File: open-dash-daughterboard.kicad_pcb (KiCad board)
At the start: 2 copper layers, 165.5 x 107.3 mm, 161 parts, among them J4 Conn_02x06_Odd_Even, P1 CONN_01X04, P2 CONN_01X02, P4 CONN_01X04, Q1 Q_NPN_BEC, Q2 Q_NJFET_DGS, Q3 Q_NJFET_DGS, Q4 Q_NPN_BCE, Q5 Q_PNP_BCE, U1 LM2576-ADJ, U10 Power-Monitor-INA219, U11 TDA7297, U12 Si4740, U13 A2235-H, U14 molex-2x4-5.7mm, U15 radio-housing-mounts, U16 molex-2x4-5.7mm, U17 USB_IC-CP2104, U18 74LVC1G17SE-7, U19 OPA1662, U2 LM2576-ADJ, U3 LM2576-ADJ, U4 LM2576-ADJ, U5 REG-3.3v, U6 ESP-WROOM-32, U7 molex-2x4-5.7mm, U8 MCP2551-I_SN, U9 SI7020-A20

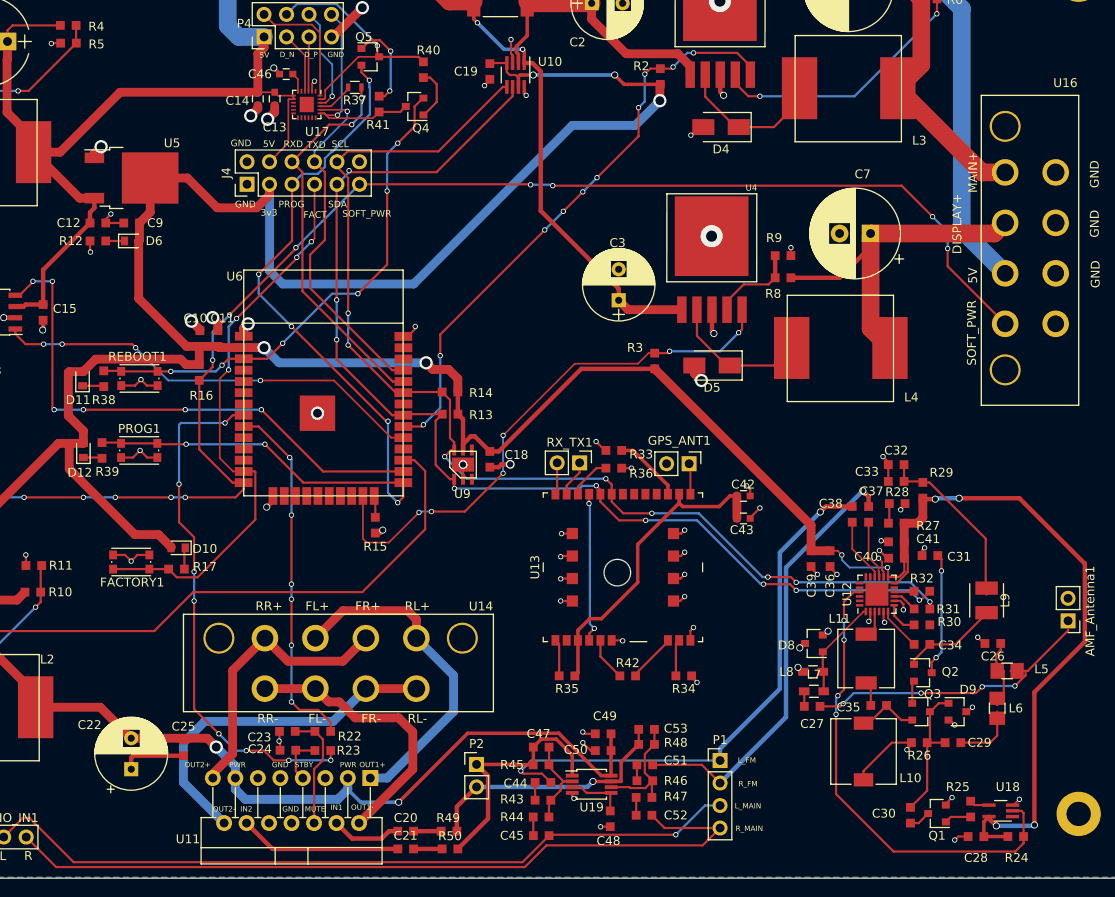
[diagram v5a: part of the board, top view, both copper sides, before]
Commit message: added softpower circuit
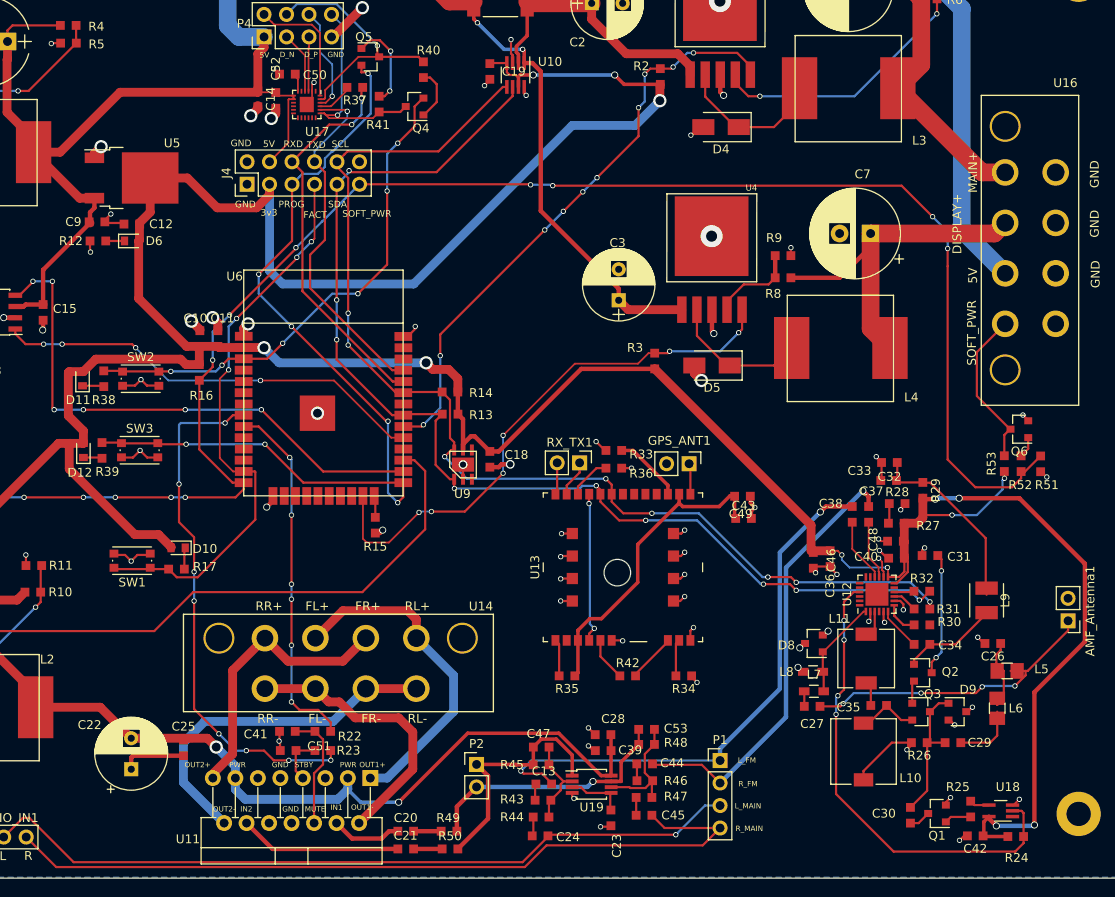
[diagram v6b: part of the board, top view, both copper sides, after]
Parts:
- removed FACTORY1, PROG1, REBOOT1: SW_PUSH, Buttons_Switches_SMD:SW_SPST_KMR2
- added Q6: Q_NPN_BEC, Package_TO_SOT_SMD:SOT-23, F.Cu at (215.3, 96.6)
- added R51: R_1k, Resistor_SMD:R_0603_1608Metric_Pad0.99x1.00mm_HandSolder, F.Cu at (217.7, 100.5)
- added R52: R_1k, Resistor_SMD:R_0603_1608Metric_Pad0.99x1.00mm_HandSolder, F.Cu at (215.5, 100.5)
- added R53: R_1k, Resistor_SMD:R_0603_1608Metric_Pad0.99x1.00mm_HandSolder, F.Cu at (213.6, 100.5)
- added SW1: SW_PUSH, Button_Switch_SMD:SW_SPST_KMR2, F.Cu at (115.1, 111.5)
- added SW2: SW_PUSH, Button_Switch_SMD:SW_SPST_KMR2, F.Cu at (116.1, 90.9)
- added SW3: SW_PUSH, Button_Switch_SMD:SW_SPST_KMR2, F.Cu at (116.0, 99.0)
- C11: value C_1uF -> C_4.7uF
- C12: value C_4.7uF -> C_1uF
- C13, C14, C43: footprint Capacitors_SMD:C_0603 -> Capacitor_SMD:C_0603_1608Metric_Pad0.99x1.00mm_HandSolder
- C15, C39: value 0.1uF -> C_0.1uF
- C25: value 100nF -> C_0.1uF
- C28, C41: value 0.1uF -> C_1uF
- C32: value 100uF -> C_47uF
- C42, C46: value C_1uF -> C_0.1uF; footprint Capacitors_SMD:C_0603 -> Capacitor_SMD:C_0603_1608Metric_Pad0.99x1.00mm_HandSolder
- C48: value C_1uF -> C_0.1uF
- C50: value C_0.1uF -> C_1uF
- R11: value R_1k3 -> R_1.3K
- R18, R24: value 4.7k -> R_4K7
- R29: value 10 -> R_10
- R37: footprint Resistors_SMD:R_0603 -> Resistor_SMD:R_0603_1608Metric_Pad0.99x1.00mm_HandSolder
- U1, U2, U3, U4: value LM2576-ADJ -> LM2576
- moved C52 90.8 mm to (131.3, 59.5), turned to 270 degrees
- moved C50 84.3 mm to (132.6, 56.5), turned to 0 degrees
- moved C13 83.1 mm to (161.6, 136.7), turned to 0 degrees
- moved C46 81.0 mm to (192.0, 111.4), turned to 270 degrees
- moved C41 72.0 mm to (132.6, 130.7), turned to 180 degrees
- moved C42 46.5 mm to (210.3, 142.5), turned to 180 degrees
- moved C48 44.9 mm to (201.3, 109.3), turned to 180 degrees
- moved C28 43.7 mm to (168.3, 131.1), turned to 180 degrees
- moved C51 40.3 mm to (132.7, 132.9)
- moved C23 37.8 mm to (169.2, 140.5), turned to 270 degrees
- moved C39 32.0 mm to (168.3, 132.9), turned to 180 degrees
- moved C49 31.1 mm to (184.0, 104.2), turned to 0 degrees
- moved C24 30.1 mm to (161.2, 142.5), turned to 0 degrees
- moved C45 11.8 mm to (172.9, 140.2), turned to 180 degrees
- moved C44 11.7 mm to (173.0, 134.4), turned to 180 degrees
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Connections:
- C12 pad 1: /5V -> /3v3
- C13 pad 1: /5V -> Net-(C13-Pad1)
- C13 pad 2: AGND -> /L_FM_AUDIO
- C19 pad 1: AGND -> /3v3
- C19 pad 2: /3v3 -> AGND
- C24 pad 2: AGND -> /L_MAIN_AUDIO
- C28 pad 1: AGND -> /AUDIO_POWER
- C28 pad 2: /3v3 -> AGND
- C32 pad 1: Net-(C32-Pad1) -> AGND
- C32 pad 2: AGND -> Net-(C32-Pad2)
- C33 pad 1: Net-(C32-Pad1) -> Net-(C32-Pad2)
- C39 pad 1: AGND -> /AUDIO_POWER
- C39 pad 2: /3v3 -> AGND
- C41 pad 1: AGND -> Net-(C41-Pad1)
- C41 pad 2: /3v3 -> AGND
- C42 pad 1: /GPS interface/3v3 -> /3v3
- C44 pad 1: Net-(C44-Pad1) -> /R_FM_AUDIO
- C44 pad 2: /L_FM_AUDIO -> Net-(C44-Pad2)
- C45 pad 1: Net-(C45-Pad1) -> /R_MAIN_AUDIO
- C45 pad 2: /L_MAIN_AUDIO -> Net-(C45-Pad2)
- C46 pad 1: AGND -> /3v3
- C46 pad 2: Net-(C46-Pad2) -> AGND
- C48 pad 1: Net-(C48-Pad1) -> /3v3
- C49 pad 1: /AUDIO_POWER -> /GPS interface/3v3
- C50 pad 1: /AUDIO_POWER -> AGND
- C50 pad 2: AGND -> Net-(C50-Pad2)
- C51 pad 1: /R_FM_AUDIO -> Net-(C51-Pad1)
- C51 pad 2: Net-(C51-Pad2) -> AGND
- C52 pad 1: /R_MAIN_AUDIO -> /5V
- C52 pad 2: Net-(C52-Pad2) -> AGND
- C9 pad 1: /3v3 -> /5V
- L9 pad 1: Net-(C32-Pad1) -> Net-(C32-Pad2)
- R22 pad 1: Net-(C23-Pad1) -> Net-(C41-Pad1)
- R23 pad 1: Net-(C24-Pad1) -> Net-(C51-Pad1)
- R29 pad 1: Net-(C32-Pad1) -> Net-(C32-Pad2)
- R43 pad 2: Net-(C44-Pad1) -> Net-(C13-Pad1)
- R44 pad 2: Net-(C45-Pad1) -> Net-(C24-Pad1)
- R46 pad 1: Net-(C51-Pad2) -> Net-(C44-Pad2)
- R47 pad 1: Net-(C52-Pad2) -> Net-(C45-Pad2)
- U11 pad 6: Net-(C23-Pad1) -> Net-(C41-Pad1)
- U11 pad 7: Net-(C24-Pad1) -> Net-(C51-Pad1)
- U16 pad 4: /SOFT_POWER -> Net-(Q6-Pad3)
- U17 pad 25: Net-(U17-Pad25) -> AGND
- U17 pad 6: Net-(C46-Pad2) -> Net-(C50-Pad2)
- U19 pad 3: Net-(C48-Pad1) -> Net-(C23-Pad1)
- U19 pad 5: Net-(C48-Pad1) -> Net-(C23-Pad1)
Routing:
- net /SOFT_POWER: track 184.5 -> 210.8 mm
- net Net-(C32-Pad2): track 0.00 -> 21.1 mm
- net Net-(C32-Pad1): track 20.2 -> 0.00 mm
- net Net-(Q6-Pad3): track 0.00 -> 17.6 mm
- net Net-(C41-Pad1): track 0.00 -> 12.9 mm
- net /3v3: track 400.2 -> 412.6 mm, vias 11 -> 13
- net Net-(C48-Pad1): track 6.75 -> 0.00 mm
- net Net-(C23-Pad1): track 13.4 -> 6.75 mm
- net Net-(C51-Pad1): track 0.00 -> 6.60 mm
- net AGND: track 152.7 -> 157.4 mm, vias 87 -> 88
- net Net-(C24-Pad1): track 6.60 -> 2.11 mm
- net Net-(U17-Pad25): track 2.47 -> 0.00 mm
- net Net-(Q6-Pad1): track 0.00 -> 2.39 mm
- net Net-(C50-Pad2): track 0.00 -> 2.17 mm
- net Net-(C46-Pad2): track 2.17 -> 0.00 mm
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
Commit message: finished schematic, starting layout
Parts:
- removed AMF_Antenna1, GPS_ANT1: Conn_01x02, Connector_PinHeader_2.54mm:PinHeader_1x02_P2.54mm_Vertical
- removed AUDIO_IN1: Conn_01x02, Connector_PinHeader_2.54mm:PinHeader_1x03_P2.54mm_Vertical
- removed C10, C13, C24, C44, C45, C51, C52: C_10uF, Capacitor_SMD:C_0603_1608Metric_Pad0.99x1.00mm_HandSolder
- removed C11, C9: C_4.7uF, Capacitor_SMD:C_0603_1608Metric_Pad0.99x1.00mm_HandSolder
- removed C12, C23, C28, C41, C49, C50: C_1uF, Capacitor_SMD:C_0603_1608Metric_Pad0.99x1.00mm_HandSolder
- removed C14, C15, C18, C19, C25, C39, C42, C43, C46, C48: C_0.1uF, Capacitor_SMD:C_0603_1608Metric_Pad0.99x1.00mm_HandSolder
- removed C16, C17: 560pF, Capacitor_SMD:C_0603_1608Metric_Pad0.99x1.00mm_HandSolder
- removed C20, C21: 0.22uF, Capacitor_SMD:C_0603_1608Metric_Pad0.99x1.00mm_HandSolder
- removed C22: 470uF, Capacitor_THT:CP_Radial_D8.0mm_P3.50mm
- removed C26: 3.9pF, Capacitor_SMD:C_0603_1608Metric_Pad0.99x1.00mm_HandSolder
- removed C27: 18pF, Capacitor_SMD:C_0603_1608Metric_Pad0.99x1.00mm_HandSolder
- removed C30: 1200pF, Capacitor_SMD:C_0603_1608Metric_Pad0.99x1.00mm_HandSolder
- removed C31, C33, C34: 0.47uF, Capacitor_SMD:C_0603_1608Metric_Pad0.99x1.00mm_HandSolder
- removed C32: C_47uF, Capacitor_SMD:C_0603_1608Metric_Pad0.99x1.00mm_HandSolder
- removed C35: 18nF, Capacitor_SMD:C_0603_1608Metric_Pad0.99x1.00mm_HandSolder
- removed C36, C40: 22nF, Capacitor_SMD:C_0603_1608Metric_Pad0.99x1.00mm_HandSolder
- removed C37, C38: 0.39uF, Capacitor_SMD:C_0603_1608Metric_Pad0.99x1.00mm_HandSolder
- removed C47, C53: C_100p, Capacitor_SMD:C_0603_1608Metric_Pad0.99x1.00mm_HandSolder
- removed C7, C8: C_1000uF, Capacitor_THT:CP_Radial_D10.0mm_P3.50mm
- removed D1: 26V Zener, Diodes_SMD:D_SMB
- removed D10, D11, D12: LED, LED_SMD:LED_0603_1608Metric_Pad0.82x1.00mm_HandSolder
- removed D2, D3, D4, D5: D_Schottky, Diode_SMD:D_SMA
- removed D6: LED-0603-G, LED_SMD:LED_0603_1608Metric_Pad0.82x1.00mm_HandSolder
- removed D8, D9: D1213A-01SO-7, TO_SOT_Packages_SMD:SOT-23
- removed L1: L_47uH, open-automation:Inductor-SRR1210
- removed L10: 1mH, Inductors_SMD:L_7.3x7.3_H4.5
- removed L11: 33uH, Inductors_SMD:L_6.3x6.3_H3
- removed L2, L3, L4: L_100uH, open-automation:Inductor-SRR1210
- removed L5, L6: 6.8uH, open-automation:Coilcraft_0805PS_Handsoldering
- removed L7: 33nH, Inductors_SMD:L_0603_HandSoldering
- removed L8: 122nH, Inductors_SMD:L_0603_HandSoldering
- removed L9: 220uH, open-automation:Coilcraft_1008PS_Handsoldering
- removed P4: CONN_01X04, Connector_PinHeader_2.54mm:PinHeader_2x04_P2.54mm_Vertical
- removed Q3: Q_NJFET_DGS, TO_SOT_Packages_SMD:SOT-23
- removed Q4: Q_NPN_BCE, Package_TO_SOT_SMD:SOT-23
- removed Q5: Q_PNP_BCE, Package_TO_SOT_SMD:SOT-23
- removed Q6: Q_NPN_BEC, Package_TO_SOT_SMD:SOT-23
- removed R10: R_7k15, Resistor_SMD:R_0603_1608Metric_Pad0.99x1.00mm_HandSolder
- removed R11: R_1.3K, Resistor_SMD:R_0603_1608Metric_Pad0.99x1.00mm_HandSolder
- removed R12: R_1k4, Resistor_SMD:R_0603_1608Metric_Pad0.99x1.00mm_HandSolder
- removed R13, R14, R15, R16, R17, R22, R23, R33, R34, R35, R36, R38, R39, R42: R_10k, Resistor_SMD:R_0603_1608Metric_Pad0.99x1.00mm_HandSolder
- removed R18, R24: R_4K7, Resistor_SMD:R_0603_1608Metric_Pad0.99x1.00mm_HandSolder
- removed R19, R20: 100, Resistor_SMD:R_0603_1608Metric_Pad0.99x1.00mm_HandSolder
- removed R21: R_10, Resistor_SMD:R_2512_6332Metric_Pad1.49x3.40mm_HandSolder
- removed R25, R27, R28: 249, Resistor_SMD:R_0603_1608Metric_Pad0.99x1.00mm_HandSolder
- removed R26: 10M, Resistor_SMD:R_0603_1608Metric_Pad0.99x1.00mm_HandSolder
- removed R29: R_10, Resistor_SMD:R_0603_1608Metric_Pad0.99x1.00mm_HandSolder
- removed R30, R31, R32: 2k, Resistor_SMD:R_0603_1608Metric_Pad0.99x1.00mm_HandSolder
- removed R37: R_470, Resistor_SMD:R_0603_1608Metric_Pad0.99x1.00mm_HandSolder
- removed R40, R41: R_12k, Resistor_SMD:R_0603_1608Metric_Pad0.99x1.00mm_HandSolder
- removed R43, R44, R45, R46, R47, R48, R49, R50: R_20k, Resistor_SMD:R_0603_1608Metric_Pad0.99x1.00mm_HandSolder
- removed R5: R_2k32, Resistor_SMD:R_0603_1608Metric_Pad0.99x1.00mm_HandSolder
- removed R51, R52, R53, R7, R9: R_1k, Resistor_SMD:R_0603_1608Metric_Pad0.99x1.00mm_HandSolder
- removed R8: R_8k87, Resistor_SMD:R_0603_1608Metric_Pad0.99x1.00mm_HandSolder
- removed RX_TX1: CONN_01X02, Connector_PinHeader_2.54mm:PinHeader_1x02_P2.54mm_Vertical
- removed SW1, SW2, SW3: SW_PUSH, Button_Switch_SMD:SW_SPST_KMR2
- removed U10: Power-Monitor-INA219, TO_SOT_Packages_SMD:SOT-23-8_Handsoldering
- removed U11: TDA7297, Package_TO_SOT_THT:TO-220-15_Vertical_StaggeredType1_Py5.08mm
- removed U14, U16: molex-2x4-5.7mm, open-automation:molex-2x4-5.7mm
- removed U15: radio-housing-mounts, open-automation:radio-housing-mounts
- removed U17: USB_IC-CP2104, Housings_DFN_QFN:QFN-24-1EP_3x3mm_Pitch0.4mm
- removed U18: 74LVC1G17SE-7, TO_SOT_Packages_SMD:SOT-353_SC-70-5_Handsoldering
- removed U19: OPA1662, Package_SO:MSOP-8_3x3mm_P0.65mm
- removed U9: SI7020-A20, open-automation:SI7020-A20
- added J1: RCA-PJRAN1X1U04X, open-automation:RCA-PJRAN1X1U04X, F.Cu at (114.8, 294.8)
- added J2: AudioJack4_TTRS, open-automation:AudioConn-SJ1-2503A, F.Cu at (150.5, 265.8)
- added J3: AudioJack4_TTRS, open-automation:AudioConn-SJ1-2503A, F.Cu at (165.0, 253.6)
- added J5: Barrel_Jack_OD5.5_ID2.5, open-automation:BarrelJack_OD5.5_ID2.5, F.Cu at (161.5, 222.7)
- added J6: Barrel_Jack_OD5.5_ID2.5, open-automation:BarrelJack_OD5.5_ID2.5, F.Cu at (161.5, 235.4)
- added J7: Conn_02x05_Odd_Even, Connector_PinHeader_2.54mm:PinHeader_2x05_P2.54mm_Vertical, F.Cu at (-22.5, 329.5)
- added J8: AudioJack4_TTRS, open-automation:AudioConn-SJ1-2503A, F.Cu at (12.7, 342.2)
- added J9: AudioJack4_TTRS, open-automation:AudioConn-SJ1-2503A, F.Cu at (25.6, 342.2)
- added U?1: ACS711, open-automation:ACS711KEXLT-15AB-T, F.Cu at (181.1, 220.0)
- C1, C2: value 180uF -> C_47pF; footprint Capacitors_THT:CP_Radial_D8.0mm_P3.50mm -> Capacitor_SMD:C_0603_1608Metric_Pad1.05x0.95mm_HandSolder
- C29: value 270pF -> 470uF; footprint Capacitor_SMD:C_0603_1608Metric_Pad0.99x1.00mm_HandSolder -> Capacitor_THT:CP_Radial_D8.0mm_P3.50mm
- C3: value 180uF -> C_0.1uF; footprint Capacitors_THT:CP_Radial_D8.0mm_P3.50mm -> Capacitor_SMD:C_0603_1608Metric_Pad1.05x0.95mm_HandSolder
- C4: value 180uF -> C_4.7uF; footprint Capacitors_THT:CP_Radial_D8.0mm_P3.50mm -> Capacitor_SMD:C_0603_1608Metric_Pad1.05x0.95mm_HandSolder
- C5: value 1000uF -> C_0.1uF; footprint Capacitors_THT:CP_Radial_D10.0mm_P5.00mm -> Capacitor_SMD:C_0603_1608Metric_Pad1.05x0.95mm_HandSolder
- C6: value 1000uF -> C_1000uF; footprint Capacitors_THT:CP_Radial_D10.0mm_P5.00mm -> Capacitor_THT:CP_Radial_D12.5mm_P5.00mm
- J4: value Conn_02x06_Odd_Even -> USB_MINI_B; footprint Connector_PinHeader_2.54mm:PinHeader_2x06_P2.54mm_Vertical -> open-automation:USB-mini-B-0548190519
- P2: value CONN_01X02 -> CONN_01X04; footprint Connector_PinHeader_2.54mm:PinHeader_1x02_P2.54mm_Vertical -> Connector_PinHeader_2.54mm:PinHeader_1x04_P2.54mm_Vertical
- Q1: value Q_NPN_BEC -> Q_NPN_BCE; footprint TO_SOT_Packages_SMD:SOT-23 -> Package_TO_SOT_SMD:SOT-23
- Q2: value Q_NJFET_DGS -> Q_PNP_BCE; footprint TO_SOT_Packages_SMD:SOT-23 -> Package_TO_SOT_SMD:SOT-23
- R1, R2: value R_10k -> R_27; footprint Resistor_SMD:R_0603_1608Metric_Pad0.99x1.00mm_HandSolder -> Resistor_SMD:R_0603_1608Metric_Pad1.05x0.95mm_HandSolder
- R3: footprint Resistor_SMD:R_0603_1608Metric_Pad0.99x1.00mm_HandSolder -> Resistor_SMD:R_0603_1608Metric_Pad1.05x0.95mm_HandSolder
- R4: value R_7k15 -> R_10k; footprint Resistor_SMD:R_0603_1608Metric_Pad0.99x1.00mm_HandSolder -> Resistor_SMD:R_0603_1608Metric_Pad1.05x0.95mm_HandSolder
- R6: value R_8k87 -> R_4K7; footprint Resistor_SMD:R_0603_1608Metric_Pad0.99x1.00mm_HandSolder -> Resistor_SMD:R_0603_1608Metric_Pad1.05x0.95mm_HandSolder
- U1: value LM2576 -> TE-AUTO-CONN-52; footprint open-automation:Regulator-LM2576 -> Connector_PinHeader_2.54mm:PinHeader_2x27_P2.54mm_Horizontal
- U12: value Si4740 -> SI7020-A20; footprint Housings_DFN_QFN:QFN-24-1EP_4x4mm_Pitch0.5mm -> open-automation:SI7020-A20
- U13: value A2235-H -> TDA7851F; footprint digikey-footprints:GSM_Module_17.8x16.5mm_A2235-H -> open-automation:Flexiwatt25-V
- U2: value LM2576 -> radio-housing-mounts; footprint open-automation:Regulator-LM2576 -> open-automation:radio-housing-mounts
- U3: value LM2576 -> ANTENNA-COAX-AUTO; footprint open-automation:Regulator-LM2576 -> open-automation:ANTENNA-AUTO- 638817-4
- U4: value LM2576 -> RDA5807M; footprint open-automation:Regulator-LM2576 -> open-automation:RDA5807M
- U7: value molex-2x4-5.7mm -> FT231XS; footprint open-automation:molex-2x4-5.7mm -> Package_SO:SSOP-20_3.9x8.7mm_P0.635mm
- moved U12 318.3 mm to (-22.0, 344.1), turned to 0 degrees
- moved C2 311.8 mm to (53.1, 338.8)
- moved R6 311.8 mm to (74.1, 331.0)
- moved U6 302.8 mm to (-44.4, 336.5)
- moved R2 294.5 mm to (74.0, 333.5), turned to 0 degrees
- moved C5 287.8 mm to (65.5, 338.4), turned to 0 degrees
- moved R4 287.1 mm to (69.7, 335.5)
- moved U8 285.1 mm to (13.4, 355.2), turned to 0 degrees
- moved D7 275.3 mm to (20.5, 353.8), turned to 0 degrees
- moved J4 275.2 mm to (61.1, 335.8), turned to 0 degrees
- moved U13 272.1 mm to (11.2, 332.8), turned to 0 degrees
- moved C29 271.6 mm to (38.2, 344.2)
- moved R3 270.1 mm to (69.9, 338.0), turned to 0 degrees
- moved C4 269.8 mm to (69.7, 333.0), turned to 0 degrees
- moved C3 264.4 mm to (74.1, 328.4), turned to 0 degrees
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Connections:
- C1 pad 1: /BATTERY -> /USB interface/USBDM
- C1 pad 2: AGND -> GND
- C2 pad 1: /V_MAIN -> /USB interface/USBDP
- C2 pad 2: AGND -> GND
- C29 pad 1: Net-(C29-Pad1) -> GND
- C29 pad 2: Net-(C29-Pad2) -> /BATTERY
- C3 pad 1: /BATTERY -> /USB interface/3V3OUT
- C3 pad 2: AGND -> GND
- C4 pad 1: /BATTERY -> /5V
- C4 pad 2: AGND -> GND
- C5 pad 2: AGND -> GND
- C6 pad 1: /MAIN_POWER -> /BATTERY
- C6 pad 2: AGND -> GND
- D7 pad 3: AGND -> GND
- J4 pad 1: AGND -> /USB interface/VBUS
- J4 pad 2: AGND -> /USB interface/USBDP
- J4 pad 3: /3v3 -> /USB interface/USBDM
- J4 pad 4: /5V -> Net-(J4-Pad4)
- J4 pad 5: /PROG -> GND
- P1 pad 1: /L_FM_AUDIO -> GND
- P1 pad 2: /R_FM_AUDIO -> /3V3
- P1 pad 3: /L_MAIN_AUDIO -> /5V
- P1 pad 4: /R_MAIN_AUDIO -> /BATTERY
- P2 pad 1: /audio amplifier/L_AUDIO_IN -> /audio amplifier/IN4
- P2 pad 2: /audio amplifier/R_AUDIO_IN -> /audio amplifier/IN3
- Q1 pad 2: AGND -> /EN_ESP
- Q1 pad 3: Net-(C30-Pad1) -> /USB interface/RTS
- Q2 pad 1: Net-(C34-Pad1) -> Net-(Q2-Pad1)
- Q2 pad 2: Net-(Q2-Pad2) -> /PROG
- Q2 pad 3: Net-(C31-Pad2) -> /USB interface/DTR
- R1 pad 1: /3v3 -> Net-(R1-Pad1)
- R1 pad 2: /EN_AUDIO -> /USB interface/USBDM
- R2 pad 1: /3v3 -> Net-(R2-Pad1)
- R2 pad 2: /EN_MAIN -> /USB interface/USBDP
- R3 pad 1: /3v3 -> (no net)
- R3 pad 2: /EN_DISPLAY -> Net-(Q2-Pad1)
- R4 pad 1: /5V -> (no net)
- R4 pad 2: Net-(R4-Pad2) -> /USB interface/DTR
- R6 pad 1: /MAIN_POWER -> /USB interface/VSENSE
- R6 pad 2: Net-(R6-Pad2) -> /USB interface/VBUS
- U1 pad 1: /BATTERY -> (no net)
- U1 pad 2: Net-(D2-Pad1) -> /CAN+
- U1 pad 3: AGND -> (no net)
- U1 pad 4: Net-(R4-Pad2) -> (no net)
- U1 pad 5: AGND -> (no net)
- U12 pad 1: Net-(D8-Pad1) -> /SDA
- U12 pad 2: AGND -> GND
- U12 pad 3: Net-(L11-Pad1) -> (no net)
- U12 pad 4: Net-(U12-Pad4) -> (no net)
- U12 pad 5: AGND -> /3V3
- U12 pad 6: Net-(C34-Pad2) -> /SCL
- U13 pad 1: /GPS interface/RST_GPS -> GND
- U13 pad 11: /GPS interface/3v3 -> Net-(C23-Pad2)
- U13 pad 13: Net-(U13-Pad13) -> GND
- U13 pad 17: /SCL -> /LR+
- U13 pad 19: /GPS interface/WAKEUP -> /LR-
- U13 pad 21: Net-(RX_TX1-Pad1) -> /RR+
- U13 pad 23: AGND -> /RR-
- U13 pad 3: /GPS interface/3v3 -> /RF-
- U13 pad 5: /GPS interface/Vout -> /RF+
- U13 pad 7: Net-(R42-Pad2) -> /LF-
- U13 pad 9: AGND -> /LF+
- U3 pad 1: /V_MAIN -> /FM Radio/AMF_Antenna
- U3 pad 2: Net-(D4-Pad1) -> GND
- U4 pad 1: /BATTERY -> /SDA
- U4 pad 2: Net-(D5-Pad1) -> /SCL
- U4 pad 3: AGND -> (no net)
- U4 pad 4: Net-(R8-Pad2) -> (no net)
- U4 pad 5: /EN_DISPLAY -> /3V3
- U5 pad 1: AGND -> GND
- U5 pad 2: /3v3 -> /3V3
- U6 pad 1: AGND -> GND
- U6 pad 13: /FACTORY -> /microcontroller/FACT
- U6 pad 14: /SOFT_POWER -> /microcontroller/SOFT_POWER
- U6 pad 2: /3v3 -> /3V3
- U6 pad 23: /EN_DISPLAY -> /DISPLAY_EN
- U6 pad 27: /EN_AUDIO -> /microcontroller/AUDIO
- U6 pad 28: Net-(U6-Pad28) -> /CAN_RX
- U6 pad 3: /EN_ESP -> /microcontroller/EN
- U6 pad 30: /EN_MAIN -> /MAIN_EN
- U7 pad 1: /BATTERY -> /USB interface/DTR
- U7 pad 2: /SOFT_POWER -> /USB interface/RTS
- U7 pad 3: /interface/CAMERA+ -> /USB interface/3V3OUT
- U7 pad 4: /CAN+ -> /RXD
- U7 pad 5: /CAN- -> Net-(U7-Pad5)
- U7 pad 6: /interface/CAMERA- -> GND
- U7 pad 7: /interface/CAMERA_S -> /USB interface/DSR
- U7 pad 8: AGND -> /USB interface/DCD
- U8 pad 2: AGND -> GND
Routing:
- net /3v3: track 412.6 -> 0.00 mm, vias 13 -> 0
- net /BATTERY: track 233.5 -> 0.00 mm, vias 2 -> 0
- net /5V: track 223.0 -> 0.00 mm
- net /SOFT_POWER: track 210.8 -> 0.00 mm, vias 14 -> 0
- net AGND: track 157.4 -> 0.00 mm, vias 88 -> 0
- net /SDA: track 129.8 -> 0.00 mm, vias 9 -> 0
- net /SCL: track 128.8 -> 0.00 mm, vias 8 -> 0
- net /AUDIO_POWER: track 108.9 -> 0.00 mm, vias 2 -> 0
- net /PROG: track 102.0 -> 0.00 mm, vias 7 -> 0
- net /R_MAIN_AUDIO: track 89.9 -> 0.00 mm
- net /EN_AUDIO: track 89.6 -> 0.00 mm, vias 2 -> 0
- net /L_MAIN_AUDIO: track 86.5 -> 0.00 mm, vias 1 -> 0
- net /EN_MAIN: track 66.8 -> 0.00 mm, vias 10 -> 0
- net /FACTORY: track 64.5 -> 0.00 mm, vias 4 -> 0
- net /L_FM_AUDIO: track 63.5 -> 0.00 mm, vias 2 -> 0
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- removed copper zone on B.Cu, net AGND
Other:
- board text removed: "3v3"
- board text removed: "5V"
- board text removed: "BATTERY"
- board text removed: "CAM-"
- board text removed: "CAMERA+"
- board text removed: "CAM_S"
- board text removed: "CAN+"
- board text removed: "CAN-"
- board text removed: "DCD"
- board text removed: "DISPLAY+"
- board text removed: "DSR"
- board text removed: "DTR"
- board text removed: "D_N"
- board text removed: "D_P"
- board text removed: "FACT"
- board text removed: "FL+"
- board text removed: "FL-"
- board text removed: "FR+"
- board text removed: "FR-"
- board text removed: "GND"
- board text removed: "IN1"
- board text removed: "IN2"
- board text removed: "L"
- board text removed: "L_FM"
- board text removed: "L_MAIN"
- board text removed: "MAIN+"
- board text removed: "MUTE"
- board text removed: "OUT1+"
- board text removed: "OUT1-"
- board text removed: "OUT2+"
- board text removed: "OUT2-"
- board text removed: "PROG"
- board text removed: "PWR"
- board text removed: "R"
- board text removed: "RL+"
- board text removed: "RL-"
- board text removed: "RR+"
- board text removed: "RR-"
- board text removed: "RTS"
- board text removed: "RXD"
- board text removed: "R_FM"
- board text removed: "R_MAIN"
- board text removed: "SCL"
- board text removed: "SDA"
- board text removed: "SOFT_PWR"
- board text removed: "STBY"
- board text removed: "TXD"
